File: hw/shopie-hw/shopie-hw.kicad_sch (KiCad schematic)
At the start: 37 parts, among them J1 Jack-DC, J2 USB_B_Micro, J3 Conn_01x04_Socket, SW1 SW_SPDT, SW2 SW_MEC_5E, SW3 SW_SPDT, U2 STM32F405RGT6, U3 LM2596T-5, U4 AP2112K-3.3, Y2 Crystal_Small

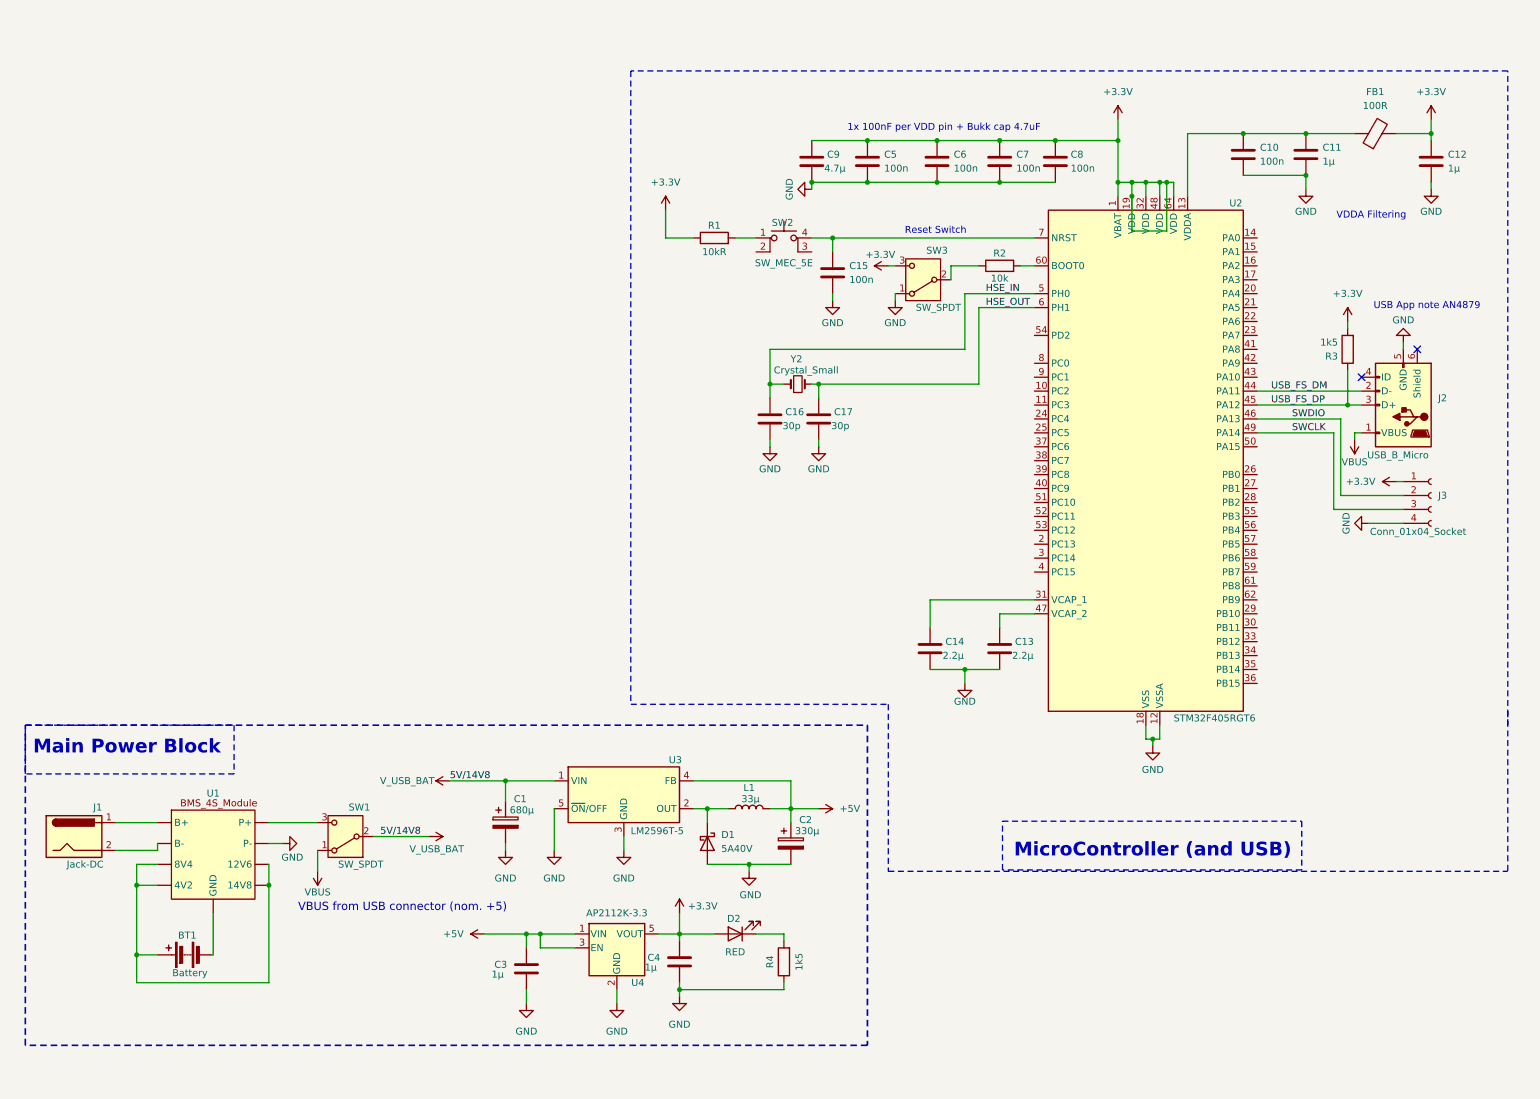
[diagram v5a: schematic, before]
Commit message: Add ICM-20948 sensor circuit, Add 1.8V regulator to main power block
- Added Sensors and Peripherals Sheet.
- Added the ICM-20948 IMU circuitry, including SPI connections to the MCU.
- Configured INT and FSYNC pins.
- Added a 1.8V voltage regulator into the main power block to supply the IMU’s required voltage for I/O logic.
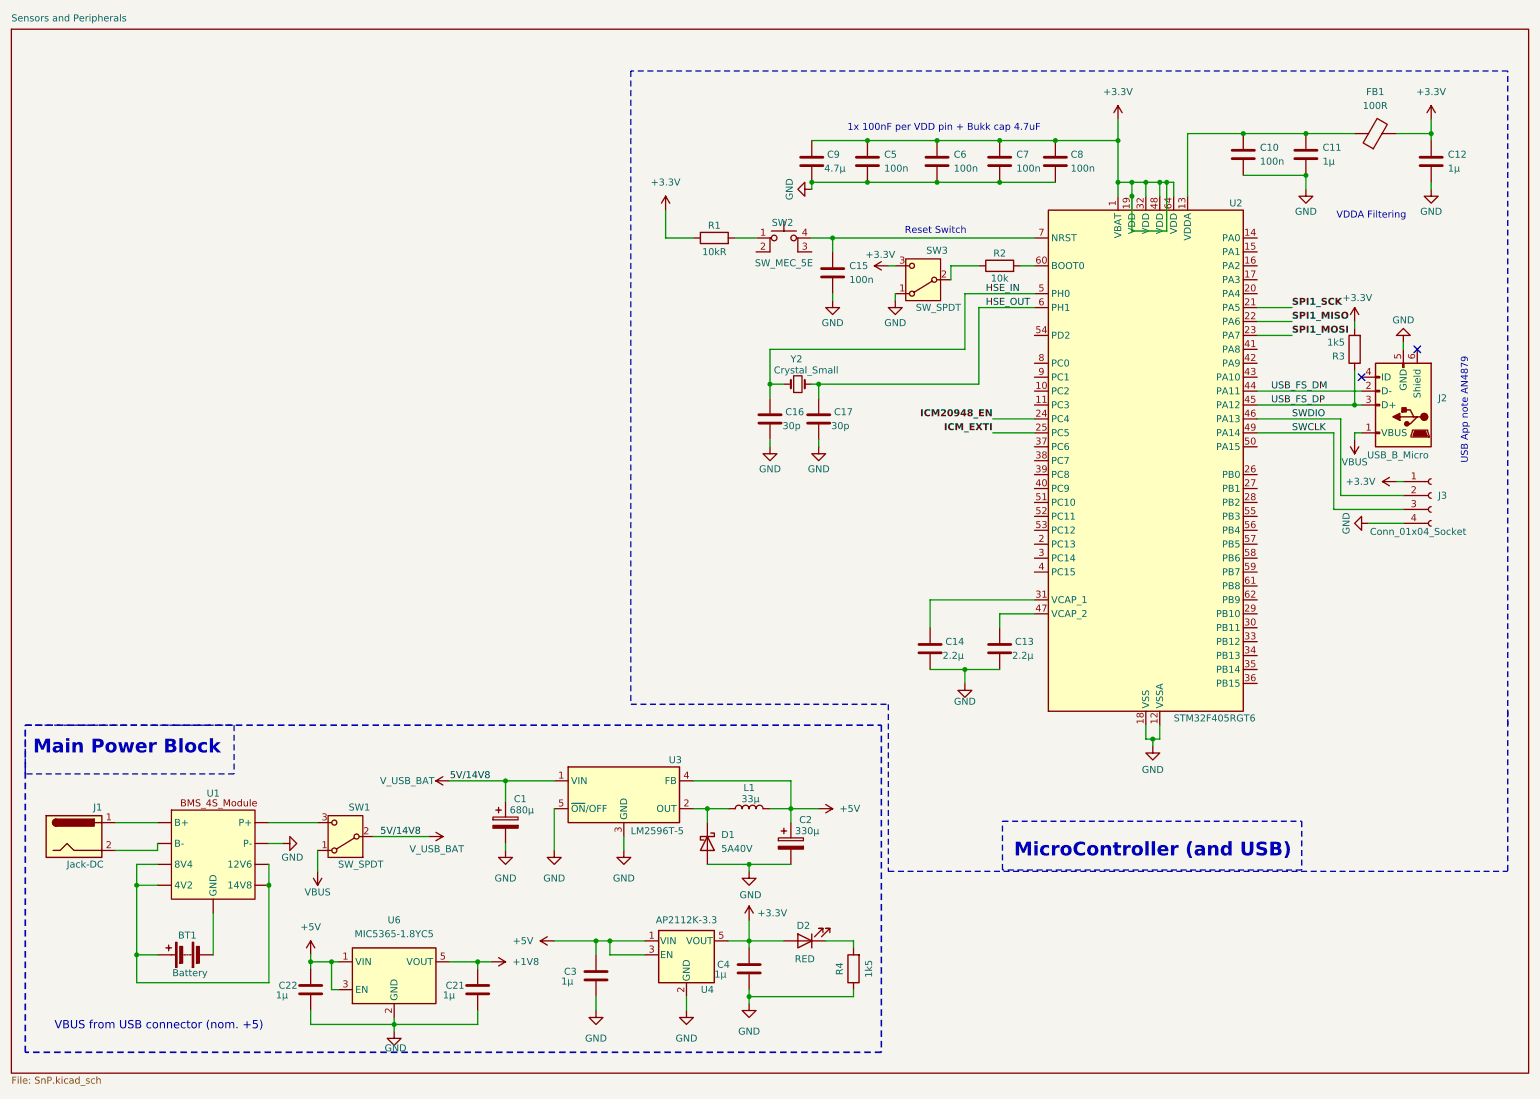
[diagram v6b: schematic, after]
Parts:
- added C21, C22: 1µ, symbol Device:C
- added U6: MIC5365-1.8YC5, Package_TO_SOT_SMD:SOT-353_SC-70-5, symbol Regulator_Linear:MIC5365-1.8YC5
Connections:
- net +5V: now also C22.1, U6.1 (VIN), U6.3 (EN)
- net GND: now also C21.2, C22.2, U6.2 (GND)
- net SPI1_SCK: now reaches U2.21 (PA5)
- net SPI1_MISO: now reaches U2.22 (PA6)
- net SPI1_MOSI: now reaches U2.23 (PA7)
- net ICM20948_EN: now reaches U2.24 (PC4)
- net ICM_EXTI: now reaches U2.25 (PC5)
- new net +1V8: C21.1, U6.5 (VOUT)
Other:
- added sheet Sensors and Peripherals (SnP.kicad_sch)
- moved on the sheet: C3, C4, D2, R3, R4, U4

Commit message: Add TMF8801 ToF Sensor
- Added TMF8801 ToF sensor symbol to schematic (SnP Sheet)
- Connected TMF8801 to STM32 MCU via I2C (SCL, SDA) and INT to EXTI-GPIO
- Connected EN pin to MCU
- Added 100nF decoupling capacitors to VDD, VDDC and VDDV as per datasheet recommendation
- Included pull-up resistors to 1.8V on SDA, SCL, and INT lines
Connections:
- net SPI2_MISO: now reaches U2.10 (PC2)
- net SPI2_MOSI: now reaches U2.11 (PC3)
- net BMP388_EXTI: now reaches U2.2 (PC13)
- net TMF8801_EXTI: now reaches U2.28 (PB2)
- net SPI2_SCK: now reaches U2.29 (PB10)
- net BMP388_EN: now reaches U2.3 (PC14)
- net I2C1_SCL: now reaches U2.58 (PB6)
- net I2C2_SDA: now reaches U2.59 (PB7)
- net TMF8801_EN: now reaches U2.8 (PC0)
- net +3.3V renamed +3V3
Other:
- moved on the sheet: C16, C17, J2, J3, R3, Y2

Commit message: Add ESP32 module to schematic and STM32 IOC pinout
- Added ESP32 (Arduino Nano ESP32 WROOM32) module symbol and footprint to the schematic
- Connected communication lines (UART/SPI/I2C as planned) between ESP32 and STM32 MCU
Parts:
- added A1: Arduino_Nano_ESP32, Module:Arduino_Nano, symbol MCU_Module:Arduino_Nano_ESP32
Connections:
- net +5V: now also A1.30 (VIN)
- net GND: now also A1.29 (GND), A1.4 (GND)
- net I2C1_SCL: now also U2.61 (PB8); no longer U2.58 (PB6)
- net TIM5_CH1: now reaches U2.14 (PA0)
- net USART2_TX: now reaches U2.16 (PA2)
- net USART2_TX: now also A1.1 (D1/TX)
- net USART2_RX: now reaches U2.17 (PA3)
- net USART2_RX: now also A1.2 (D0/RX)
- net TIM3_CH1: now reaches U2.37 (PC6)
- net TIM2_CH1: now reaches U2.50 (PA15)
- new net TIM4_CH1: U2.58 (PB6)
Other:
- sheet Sensors and Peripherals renamed MCU, Power, Communication
- note added: "Communication"
- note added: "ESP32 is used for communication only due to it's simpliest and availbity. In future this would be change to something more powerfull to handle AI models"
